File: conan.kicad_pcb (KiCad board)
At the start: 2 copper layers, 307 parts, among them J1 JST-XH, J10 PWM11, J11 PWM3, J12 PWM7, J13 PWM12, J14 PWM4, J15 PWM8, J16 Stepper, J17 Stepper, J18 Stepper, J19 Stepper, J2 JST-XH, J20 Stepper, J21 Stepper, J22 Boot, J23 UART1, J24 UART2, J25 USB_B_Micro, J26 Endstop 1, J27 Endstop 2, J28 Endstop 3, J29 Endstop 4, J3 JTAG, J30 Endstop 5, J31 Endstop 6, J32 Endstop 7, J33 Endstop 8, J34 Watchdog, J35 Thermistor 1, J36 Thermistor 2, J37 Thermistor 3, J38 Thermistor 4, J39 Thermistor 5, J4 PWM9, J40 Thermistor 6, J41 Thermistor 7, J42 Thermistor 8, J43 pmod, J44 esp8266, J45 Chain_in, J46 Chain_out, J47 Exp1_L, J48 Display, J49 Exp1_R, J5 PWM5, J50 Vaux in, J51 VM2 in, J52 VM1 in, J53 Vaux in, J54 Exp2_L, J55 Exp2_R, J6 PWM1_HP, J7 PWM10, J8 PWM2_HP, J9 PWM6, Q1 AON7524, Q2 TPH1R405PL, Q3 TPH1R405PL, Q4 AON7524, Q5 AON7524, Q6 AON7524, Q7 AON7524, Q8 AON7524, Q9 Q_NMOS_DGS, SW1 Reset, U1 ECP5U12_CABGA256, U10 TMC2209, U11 TMC2209, U12 TMC2209, U13 TMC2209, U14 AT25xxx, U15 STM32F070CBTx, U16 74VLX244, U17 STWD100, U2 L7986, U3 TLV62569, U4 TLV62569, U5 LP5907MFX-2.5, U6 LP5907MFX-3.3, U7 MIC4127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

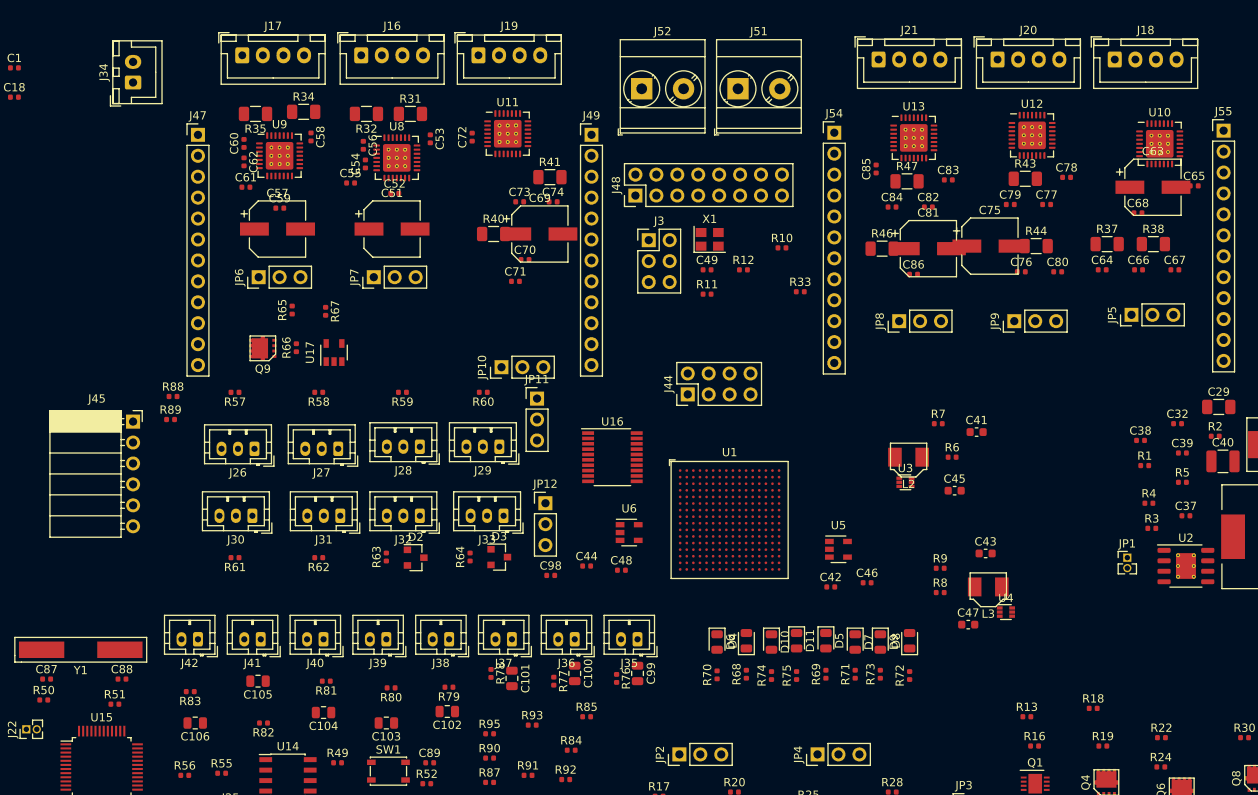
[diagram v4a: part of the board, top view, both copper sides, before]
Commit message: routing sketch for stepper driver
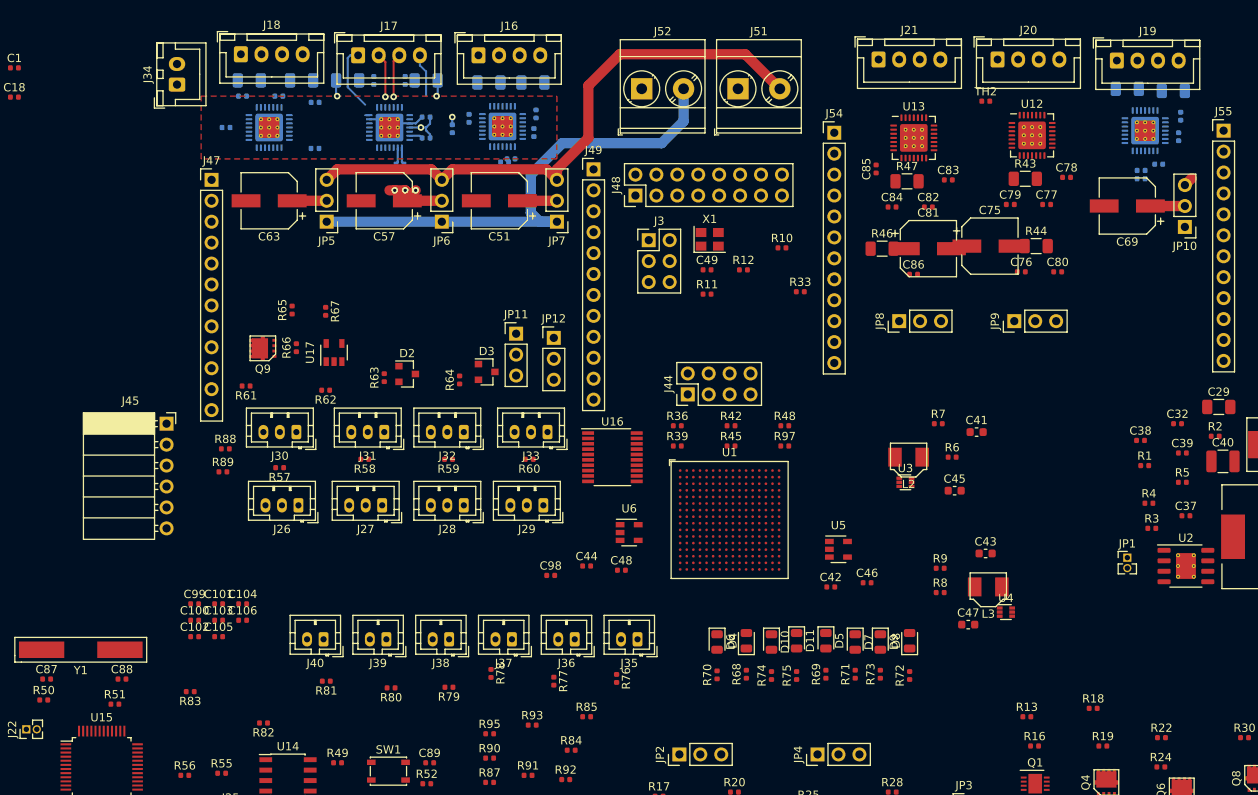
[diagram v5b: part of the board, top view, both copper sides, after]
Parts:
- removed J41: Thermistor 7, Connector_JST:JST_PH_B2B-PH-K_1x02_P2.00mm_Vertical
- removed J42: Thermistor 8, Connector_JST:JST_PH_B2B-PH-K_1x02_P2.00mm_Vertical
- added R36: 1k, Resistor_SMD:R_0402_1005Metric, F.Cu at (115.6, 72.4)
- added R39: 1k, Resistor_SMD:R_0402_1005Metric, F.Cu at (115.6, 74.8)
- added R42: 1k, Resistor_SMD:R_0402_1005Metric, F.Cu at (122.1, 72.4)
- added R45: 1k, Resistor_SMD:R_0402_1005Metric, F.Cu at (122.1, 74.8)
- added R48: 1k, Resistor_SMD:R_0402_1005Metric, F.Cu at (128.6, 72.4)
- added R97: 1k, Resistor_SMD:R_0402_1005Metric, F.Cu at (128.6, 74.8)
- added TH1: NTC_100k, Resistor_SMD:R_0402_1005Metric, B.Cu at (88.3, 36.3)
- added TH2: NTC_100k, Resistor_SMD:R_0402_1005Metric, F.Cu at (153.0, 33.0)
- C100, C101, C102, C103, C104, C99: value 10uF -> 2.2uF; footprint Capacitor_SMD:C_0805_2012Metric -> Capacitor_SMD:C_0402_1005Metric
- C105, C106: value 10uF -> 1uF; footprint Capacitor_SMD:C_0805_2012Metric -> Capacitor_SMD:C_0402_1005Metric
- C52, C53, C54, C55, C56, C58, C59, C60, C61, C62, C64, C65, C66, C67, C68, C70, C71, C72, C73, C74, R31, R32, R34, R35, R37, R38, R40, R41, U10, U11, U8, U9: moved to B.Cu
- moved C65 117.7 mm to (60.8, 36.2), turned to 180 degrees
- moved C67 115.1 mm to (62.8, 32.4), turned to 180 degrees
- moved U10 108.1 mm to (66.0, 36.2), turned to 180 degrees
- moved C63 107.3 mm to (66.0, 45.1), turned to 180 degrees
- moved C66 106.4 mm to (67.2, 32.4), turned to 180 degrees
- moved J18 106.0 mm to (62.6, 27.3)
- moved R37 106.0 mm to (63.6, 30.5), turned to 180 degrees
- moved R38 105.3 mm to (70.0, 30.5), turned to 180 degrees
- moved C68 100.2 mm to (71.6, 38.7), turned to 180 degrees
- moved JP5 98.3 mm to (73.0, 47.6), turned to 180 degrees
- moved C64 97.6 mm to (71.6, 33.1), turned to 180 degrees
- moved C72 86.0 mm to (176.7, 34.8)
- moved JP10 84.7 mm to (177.2, 48.3), turned to 180 degrees
- moved R40 78.9 mm to (170.2, 31.5), turned to 180 degrees
- moved C73 77.7 mm to (174.0, 40.6), turned to 180 degrees
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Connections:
- net Net-(J16-Pad3) renamed /Stepper/Stepper 3/OB1
- net Net-(J16-Pad4) renamed /Stepper/Stepper 3/OB2
- net Net-(J17-Pad3) renamed /Stepper/Stepper 2/OB1
- net Net-(J17-Pad4) renamed /Stepper/Stepper 2/OB2
- net Net-(J18-Pad3) renamed /Stepper/Stepper 1/OB1
- net Net-(J18-Pad4) renamed /Stepper/Stepper 1/OB2
- net Net-(J19-Pad3) renamed /Stepper/Stepper 6/OB1
- net Net-(J19-Pad4) renamed /Stepper/Stepper 6/OB2
- net Net-(J20-Pad3) renamed /Stepper/Stepper 5/OB1
- net Net-(J20-Pad4) renamed /Stepper/Stepper 5/OB2
- net Net-(J21-Pad3) renamed /Stepper/Stepper 4/OB1
- net Net-(J21-Pad4) renamed /Stepper/Stepper 4/OB2
- J16 pad 1: Net-(J16-Pad1) -> /Stepper/Stepper 3/OA1
- J16 pad 2: Net-(J16-Pad2) -> /Stepper/Stepper 3/OA2
- J17 pad 1: Net-(J17-Pad1) -> /Stepper/Stepper 2/OA1
- J17 pad 2: Net-(J17-Pad2) -> /Stepper/Stepper 2/OA2
- J18 pad 1: Net-(J18-Pad1) -> /Stepper/Stepper 1/OA1
- J18 pad 2: Net-(J18-Pad2) -> /Stepper/Stepper 1/OA2
- J19 pad 1: Net-(J19-Pad1) -> /Stepper/Stepper 6/OA1
- J19 pad 2: Net-(J19-Pad2) -> /Stepper/Stepper 6/OA2
- J20 pad 1: Net-(J20-Pad1) -> /Stepper/Stepper 5/OA1
- J20 pad 2: Net-(J20-Pad2) -> /Stepper/Stepper 5/OA2
- J21 pad 1: Net-(J21-Pad1) -> /Stepper/Stepper 4/OA1
- J21 pad 2: Net-(J21-Pad2) -> /Stepper/Stepper 4/OA2
- U10 pad 14: UART1 -> Net-(R42-Pad2)
- U10 pad 21: Net-(J18-Pad1) -> /Stepper/Stepper 1/OA2
- U10 pad 24: Net-(J18-Pad2) -> /Stepper/Stepper 1/OA1
- U11 pad 14: UART6 -> Net-(R45-Pad2)
- U11 pad 21: Net-(J19-Pad1) -> /Stepper/Stepper 6/OA2
- U11 pad 24: Net-(J19-Pad2) -> /Stepper/Stepper 6/OA1
- U12 pad 14: UART5 -> Net-(R48-Pad2)
- U12 pad 21: Net-(J20-Pad1) -> /Stepper/Stepper 5/OA2
- U12 pad 24: Net-(J20-Pad2) -> /Stepper/Stepper 5/OA1
- U13 pad 14: UART4 -> Net-(R97-Pad2)
- U13 pad 21: Net-(J21-Pad1) -> /Stepper/Stepper 4/OA2
- U13 pad 24: Net-(J21-Pad2) -> /Stepper/Stepper 4/OA1
- U8 pad 14: UART3 -> Net-(R36-Pad2)
- U8 pad 21: Net-(J16-Pad1) -> /Stepper/Stepper 3/OA2
- U8 pad 24: Net-(J16-Pad2) -> /Stepper/Stepper 3/OA1
- U9 pad 14: UART2 -> Net-(R39-Pad2)
- U9 pad 21: Net-(J17-Pad1) -> /Stepper/Stepper 2/OA2
- U9 pad 24: Net-(J17-Pad2) -> /Stepper/Stepper 2/OA1
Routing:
- net +VM2: track 0.00 -> 70.8 mm
- net +VM1: track 0.00 -> 61.4 mm
- net /Stepper/Stepper 2/VM: track 0.00 -> 14.1 mm, vias 0 -> 4
- net GND: track 0.00 -> 11.9 mm, vias 0 -> 3
- net /Stepper/Stepper 2/OA1: track 0.00 -> 7.96 mm
- net /Stepper/Stepper 2/OA2: track 0.00 -> 5.88 mm, vias 0 -> 1
- net /Stepper/Stepper 2/OB1: track 0.00 -> 5.33 mm, vias 0 -> 1
- net /Stepper/Stepper 2/OB2: track 0.00 -> 5.27 mm
- net /Stepper/Stepper 6/VM: track 0.00 -> 4.19 mm
- net /Stepper/Stepper 3/VM: track 0.00 -> 4.19 mm
- net /Stepper/Stepper 1/VM: track 0.00 -> 4.19 mm
- net Net-(C61-Pad1): track 0.00 -> 2.10 mm
- net Net-(C60-Pad1): track 0.00 -> 1.62 mm
- added copper zone on In2.Cu, net /Stepper/Stepper 2/VM
- added copper zone on F.Cu, net GND
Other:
- copper layers 2 -> 4
- rule trace_min: 0.2 -> 0.09
- rule via_min_drill: 0.3 -> 0.2
- rule via_min_size: 0.4 -> 0.45

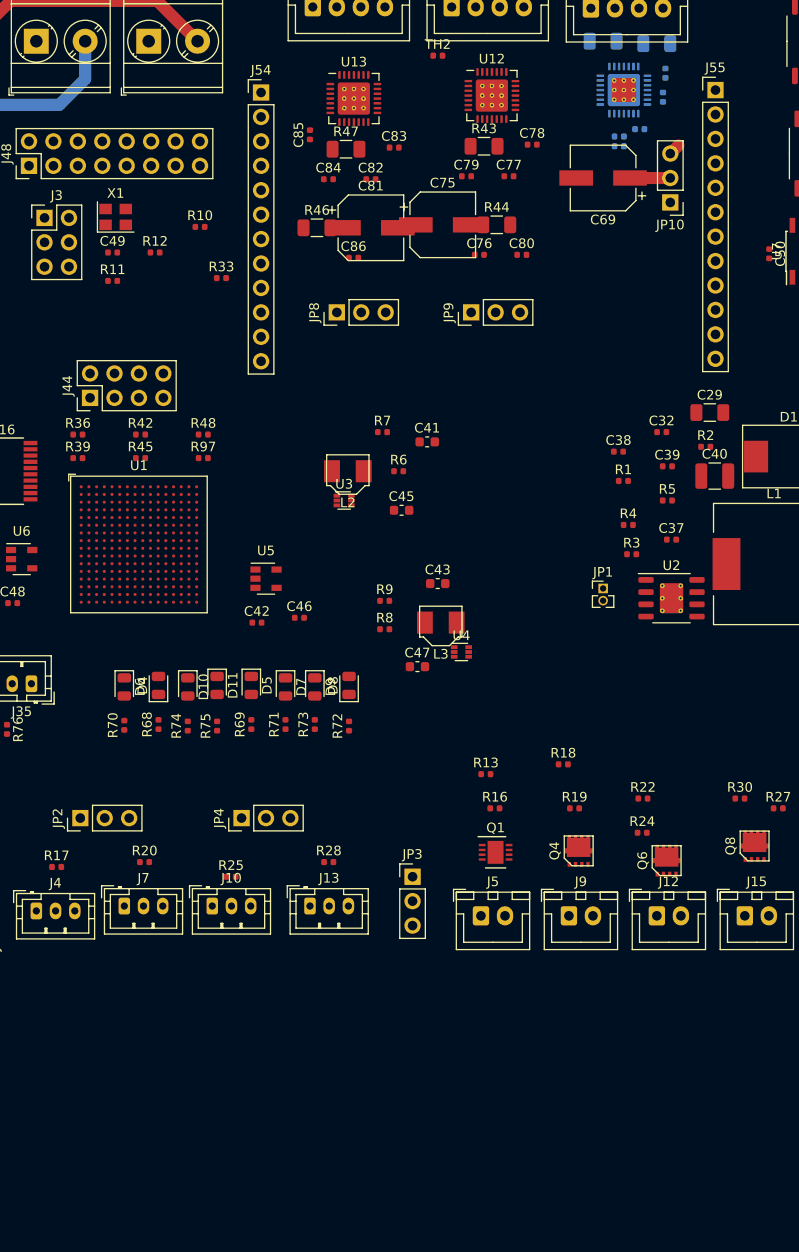
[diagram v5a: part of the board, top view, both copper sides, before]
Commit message: rough reassignment of fpga-pads to account for the direction in which the wires go. Only assign to outer 4 rings for easier escape routing.
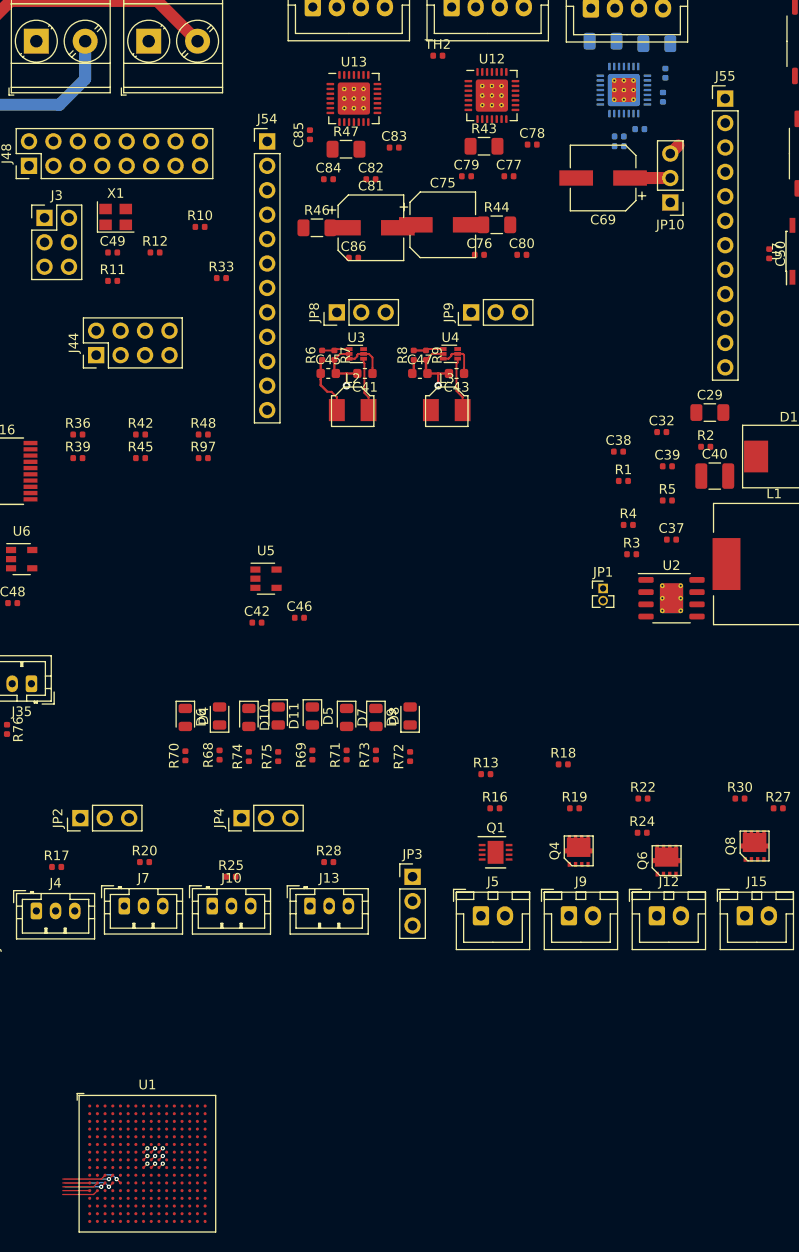
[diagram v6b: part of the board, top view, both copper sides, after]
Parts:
- moved U1 64.4 mm to (122.8, 148.2)
- moved U4 31.0 mm to (154.3, 64.0)
- moved C47 30.5 mm to (151.1, 66.0)
- moved R8 28.7 mm to (150.5, 64.1), turned to 90 degrees
- moved R9 25.9 mm to (151.8, 64.1), turned to 270 degrees
- moved L3 22.1 mm to (153.9, 69.8), turned to 180 degrees
- moved C43 21.9 mm to (154.9, 66.0), turned to 180 degrees
- moved C45 16.1 mm to (141.6, 66.0)
- moved U3 15.3 mm to (144.5, 64.0)
- moved R6 14.5 mm to (141.0, 64.1), turned to 90 degrees
- moved C41 9.62 mm to (145.4, 66.0), turned to 180 degrees
- moved R7 9.44 mm to (142.2, 64.1), turned to 270 degrees
- moved R68 7.10 mm to (130.3, 105.7)
- moved R69 7.10 mm to (140.0, 105.7)
- moved R71 7.10 mm to (143.5, 105.7)
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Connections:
- U1 pad A10: UART6 -> Net-(U1-PadA10)
- U1 pad A11: PWM11 -> Net-(U1-PadA11)
- U1 pad A12: PWM9 -> Net-(U1-PadA12)
- U1 pad A4: Net-(U1-PadA4) -> DIAG3
- U1 pad A5: Net-(U1-PadA5) -> display10
- U1 pad A6: Net-(U1-PadA6) -> display9
- U1 pad A7: Net-(U1-PadA7) -> display3
- U1 pad A8: Net-(U1-PadA8) -> display1
- U1 pad A9: FPGA2 -> Net-(U1-PadA9)
- U1 pad B1: ENDSTOP1 -> DIR1
- U1 pad B10: FPGA1 -> Net-(U1-PadB10)
- U1 pad B11: UART3 -> Net-(U1-PadB11)
- U1 pad B12: PWM8 -> Net-(U1-PadB12)
- U1 pad B13: PWM4 -> ESP_EN
- U1 pad B15: display13 -> exp2_16
- U1 pad B16: Net-(U1-PadB16) -> exp2_17
- U1 pad B2: ENDSTOP2 -> STEP1
- U1 pad B3: Net-(U1-PadB3) -> INDEX3
- U1 pad B4: Net-(U1-PadB4) -> DIAG1
- U1 pad B5: Net-(U1-PadB5) -> display11
- U1 pad B6: Net-(U1-PadB6) -> display6
- U1 pad B7: Net-(U1-PadB7) -> display2
- U1 pad B8: WDI -> Net-(U1-PadB8)
- U1 pad B9: FPGA6 -> Net-(U1-PadB9)
- U1 pad C1: ENDSTOP5 -> DIR3
- U1 pad C10: UART5 -> Net-(U1-PadC10)
- U1 pad C11: UART1 -> Net-(U1-PadC11)
- U1 pad C12: PWM6 -> ESP_GPIO2
- U1 pad C13: PWM2 -> ESP_RX
- U1 pad C14: display12 -> exp2_15
- U1 pad C15: display8 -> exp2_11
- U1 pad C16: display10 -> exp2_13
- U1 pad C2: ENDSTOP7 -> UART1
- U1 pad C3: ENDSTOP3 -> DIR2
- U1 pad C4: Net-(U1-PadC4) -> DIAG2
- U1 pad C5: Net-(U1-PadC5) -> display13
- U1 pad C6: Net-(U1-PadC6) -> display7
- U1 pad C7: Net-(U1-PadC7) -> display4
- U1 pad C8: CLK -> Net-(U1-PadC8)
- U1 pad C9: FPGA4 -> Net-(U1-PadC9)
- U1 pad D1: LED1 -> UART3
- U1 pad D10: UART4 -> Net-(U1-PadD10)
- U1 pad D11: PWM12 -> Net-(U1-PadD11)
- U1 pad D12: PWM7 -> Net-(U1-PadD12)
- U1 pad D13: PWM3 -> ESP_RST
- U1 pad D14: display11 -> exp2_14
- U1 pad D16: display6 -> exp2_9
- U1 pad D3: ENDSTOP4 -> STEP2
- U1 pad D4: Net-(U1-PadD4) -> INDEX1
- U1 pad D5: Net-(U1-PadD5) -> display12
- U1 pad D6: Net-(U1-PadD6) -> display8
- U1 pad D7: Net-(U1-PadD7) -> display5
- U1 pad D8: WDEN -> Net-(U1-PadD8)
- U1 pad D9: FPGA5 -> Net-(U1-PadD9)
- U1 pad E1: LED8 -> exp1_7
- U1 pad E10: UART2 -> Net-(U1-PadE10)
- U1 pad E11: PWM10 -> Net-(U1-PadE11)
- U1 pad E12: PWM5 -> ESP_FLASH
- U1 pad E13: PWM1 -> ESP_TX
- U1 pad E14: display9 -> exp2_12
- U1 pad E15: display4 -> exp2_7
- U1 pad E16: pmod2_2 -> exp2_2
- U1 pad E2: LED3 -> exp1_2
- U1 pad E3: ENDSTOP6 -> STEP3
- U1 pad E4: Net-(U1-PadE4) -> INDEX2
- U1 pad E8: ENN -> Net-(U1-PadE8)
- U1 pad E9: FPGA3 -> Net-(U1-PadE9)
- U1 pad F1: DIR1 -> exp1_8
- U1 pad F12: display3 -> exp2_6
- U1 pad F13: display5 -> exp2_8
- U1 pad F14: display7 -> exp2_10
- U1 pad F15: display1 -> exp2_4
- U1 pad F16: pmod2_3 -> exp2_1
- U1 pad F2: LED6 -> exp1_5
- U1 pad F3: ENDSTOP8 -> UART2
- U1 pad F4: LED2 -> exp1_1
- U1 pad F5: LED4 -> exp1_3
- U1 pad G1: STEP5 -> exp1_14
- U1 pad G12: display2 -> exp2_5
- U1 pad G13: pmod2_1 -> exp2_3
- U1 pad G14: pmod2_4 -> DIAG6
- U1 pad G15: pmod1_4 -> INDEX6
- U1 pad G16: chain_in_in3 -> UART5
- U1 pad G2: DIR2 -> exp1_10
- U1 pad G3: STEP1 -> exp1_9
- U1 pad G4: LED7 -> exp1_6
- U1 pad G5: LED5 -> exp1_4
- U1 pad H12: pmod1_2 -> INDEX5
- U1 pad H13: chain_in_in1 -> INDEX4
- U1 pad H14: pmod1_3 -> DIAG5
- U1 pad H15: chain_in_out2 -> DIR6
- U1 pad H2: STEP6 -> exp1_16
- U1 pad H3: STEP2 -> exp1_11
- U1 pad H4: STEP4 -> exp1_13
- U1 pad H5: DIR3 -> Net-(U1-PadH5)
- U1 pad J1: Net-(U1-PadJ1) -> WDI
- U1 pad J12: chain_in_in2 -> UART6
- U1 pad J13: pmod1_1 -> DIAG4
- U1 pad J14: chain_in_out1 -> UART4
- U1 pad J15: chain_out_out2 -> DIR4
- U1 pad J16: chain_out_in1 -> DIR5
- U1 pad J2: Net-(U1-PadJ2) -> CLK
- U1 pad J3: DIR5 -> exp1_15
- U1 pad J4: STEP3 -> exp1_12
- U1 pad J5: DIR4 -> Net-(U1-PadJ5)
- U1 pad K1: Net-(U1-PadK1) -> WDEN
- U1 pad K12: Net-(U1-PadK12) -> pmod1_2
- U1 pad K13: Net-(U1-PadK13) -> pmod1_4
- U1 pad K14: chain_out_in2 -> STEP6
- U1 pad K15: chain_out_out1 -> STEP4
- U1 pad K16: chain_out_out3 -> STEP5
- U1 pad K2: Net-(U1-PadK2) -> ENN
- U1 pad K3: DIR6 -> exp1_17
- U1 pad K4: exp2_5 -> PWM5
- U1 pad K5: exp2_7 -> PWM7
- U1 pad L1: exp2_1 -> PWM1
- U1 pad L12: Net-(U1-PadL12) -> pmod1_1
- U1 pad L13: Net-(U1-PadL13) -> pmod1_3
- U1 pad L14: ESP_GPIO2 -> chain_in_in2
- U1 pad L15: Net-(U1-PadL15) -> pmod2_3
- U1 pad L16: Net-(U1-PadL16) -> pmod2_1
- U1 pad L2: exp2_3 -> PWM3
- U1 pad L3: exp2_10 -> PWM10
- U1 pad L4: exp2_6 -> PWM6
- U1 pad L5: exp2_8 -> PWM8
- U1 pad M1: exp2_2 -> PWM2
- U1 pad M11: exp1_4 -> Net-(U1-PadM11)
- U1 pad M12: exp1_7 -> ENDSTOP1
- U1 pad M13: ESP_RX -> chain_out_in2
- U1 pad M14: ESP_EN -> chain_in_out1
- U1 pad M15: Net-(U1-PadM15) -> pmod2_4
- U1 pad M16: Net-(U1-PadM16) -> pmod2_2
- U1 pad M2: exp2_4 -> PWM4
- U1 pad M3: exp2_12 -> PWM12
- U1 pad M4: exp2_14 -> FPGA2
- U1 pad M5: INDEX5 -> Net-(U1-PadM5)
- U1 pad M6: DIAG6 -> Net-(U1-PadM6)
- U1 pad N1: exp2_9 -> PWM9
- U1 pad N11: exp1_3 -> Net-(U1-PadN11)
- U1 pad N12: exp1_5 -> Net-(U1-PadN12)
- U1 pad N13: exp1_16 -> chain_out_out2
- U1 pad N14: exp1_17 -> chain_out_out3
- U1 pad N16: Net-(U1-PadN16) -> chain_in_in1
- U1 pad N3: exp2_16 -> FPGA4
- U1 pad N4: exp2_17 -> FPGA5
- U1 pad N5: INDEX6 -> Net-(U1-PadN5)
- U1 pad P1: exp2_13 -> FPGA1
- U1 pad P11: exp1_2 -> Net-(U1-PadP11)
- U1 pad P12: exp1_1 -> Net-(U1-PadP12)
- U1 pad P13: exp1_12 -> ENDSTOP6
- U1 pad P14: exp1_14 -> ENDSTOP8
- U1 pad P15: ESP_FLASH -> chain_in_in3
- U1 pad P16: ESP_RST -> chain_in_out2
- U1 pad P2: exp2_11 -> PWM11
- U1 pad P3: INDEX1 -> LED1
- U1 pad P4: INDEX2 -> LED3
- U1 pad R1: exp2_15 -> FPGA3
- U1 pad R12: exp1_8 -> ENDSTOP2
- U1 pad R13: exp1_11 -> ENDSTOP5
- U1 pad R14: exp1_10 -> ENDSTOP4
- U1 pad R15: exp1_15 -> chain_out_out1
- U1 pad R16: ESP_TX -> chain_out_in1
- U1 pad R2: DIAG1 -> FPGA6
- U1 pad R3: INDEX3 -> LED5
- U1 pad R4: DIAG3 -> LED4
- U1 pad R5: DIAG4 -> LED7
- U1 pad T13: exp1_6 -> Net-(U1-PadT13)
- U1 pad T14: exp1_9 -> ENDSTOP3
- U1 pad T15: exp1_13 -> ENDSTOP7
- U1 pad T2: DIAG2 -> LED2
- U1 pad T3: INDEX4 -> LED6
- U1 pad T4: DIAG5 -> LED8
- U4 pad 5: Net-(U4-Pad5) -> +5V
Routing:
- net GND: track 11.9 -> 30.2 mm, vias 3 -> 13
- net +5V: track 0.00 -> 8.96 mm
- net +1V1: track 0.00 -> 6.80 mm, vias 0 -> 1
- net Net-(L3-Pad1): track 0.00 -> 5.66 mm
- net Net-(L2-Pad1): track 0.00 -> 5.56 mm
- net PWM6: track 0.00 -> 5.36 mm, vias 0 -> 1
- net PWM5: track 0.00 -> 5.17 mm, vias 0 -> 1
- net exp1_17: track 0.00 -> 4.57 mm
- net PWM10: track 0.00 -> 4.37 mm, vias 0 -> 1
- net PWM4: track 0.00 -> 3.77 mm
- net PWM3: track 0.00 -> 3.77 mm
- net Net-(R8-Pad2): track 0.00 -> 3.12 mm
- net Net-(R6-Pad2): track 0.00 -> 2.86 mm
- net PWM2: track 0.00 -> 2.80 mm
- net PWM1: track 0.00 -> 2.80 mm
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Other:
- net class Default: clearance 0.2 -> 0.15
- rule trace_clearance: 0.2 -> 0.15

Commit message: more reassignments
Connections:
- U1 pad A10: Net-(U1-PadA10) -> chain_in_in3
- U1 pad A9: Net-(U1-PadA9) -> chain_in_in1
- U1 pad B10: Net-(U1-PadB10) -> chain_in_in2
- U1 pad B15: exp2_16 -> exp2_12
- U1 pad B16: exp2_17 -> exp2_13
- U1 pad C10: Net-(U1-PadC10) -> chain_in_out1
- U1 pad C14: exp2_15 -> exp2_11
- U1 pad C15: exp2_11 -> exp2_7
- U1 pad C16: exp2_13 -> exp2_9
- U1 pad D10: Net-(U1-PadD10) -> chain_in_out2
- U1 pad D14: exp2_14 -> exp2_10
- U1 pad D16: exp2_9 -> exp2_5
- U1 pad E14: exp2_12 -> exp2_8
- U1 pad E15: exp2_7 -> exp2_3
- U1 pad E16: exp2_2 -> DIAG6
- U1 pad F12: exp2_6 -> Net-(U1-PadF12)
- U1 pad F13: exp2_8 -> exp2_4
- U1 pad F14: exp2_10 -> exp2_6
- U1 pad F15: exp2_4 -> exp2_2
- U1 pad F16: exp2_1 -> INDEX6
- U1 pad G12: exp2_5 -> Net-(U1-PadG12)
- U1 pad G13: exp2_3 -> exp2_1
- U1 pad G14: DIAG6 -> DIAG5
- U1 pad G15: INDEX6 -> INDEX5
- U1 pad H12: INDEX5 -> Net-(U1-PadH12)
- U1 pad H13: INDEX4 -> UART6
- U1 pad H14: DIAG5 -> DIAG4
- U1 pad J12: UART6 -> Net-(U1-PadJ12)
- U1 pad J13: DIAG4 -> INDEX4
- U1 pad K12: pmod1_2 -> Net-(U1-PadK12)
- U1 pad K5: PWM7 -> Net-(U1-PadK5)
- U1 pad L12: pmod1_1 -> Net-(U1-PadL12)
- U1 pad L14: chain_in_in2 -> pmod1_1
- U1 pad L3: PWM10 -> PWM8
- U1 pad L5: PWM8 -> Net-(U1-PadL5)
- U1 pad M12: ENDSTOP1 -> Net-(U1-PadM12)
- U1 pad M13: chain_out_in2 -> chain_out_out2
- U1 pad M14: chain_in_out1 -> chain_out_in1
- U1 pad M3: PWM12 -> PWM10
- U1 pad N1: PWM9 -> PWM7
- U1 pad N12: Net-(U1-PadN12) -> exp2_14
- U1 pad N13: chain_out_out2 -> ENDSTOP7
- U1 pad N14: chain_out_out3 -> ENDSTOP8
- U1 pad N16: chain_in_in1 -> pmod1_2
- U1 pad P11: Net-(U1-PadP11) -> PWM12
- U1 pad P12: Net-(U1-PadP12) -> PWM11
- U1 pad P13: ENDSTOP6 -> ENDSTOP3
- U1 pad P14: ENDSTOP8 -> ENDSTOP5
- U1 pad P15: chain_in_in3 -> chain_out_in2
- U1 pad P16: chain_in_out2 -> chain_out_out3
- U1 pad P2: PWM11 -> PWM9
- U1 pad R12: ENDSTOP2 -> exp2_16
- U1 pad R13: ENDSTOP5 -> ENDSTOP2
- U1 pad R14: ENDSTOP4 -> ENDSTOP1
- U1 pad R15: chain_out_out1 -> ENDSTOP6
- U1 pad R16: chain_out_in1 -> chain_out_out1
- U1 pad T13: Net-(U1-PadT13) -> exp2_15
- U1 pad T14: ENDSTOP3 -> exp2_17
- U1 pad T15: ENDSTOP7 -> ENDSTOP4
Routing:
- net PWM10: track 4.37 -> 0.00 mm, vias 1 -> 0
- net PWM8: track 1.91 -> 4.37 mm

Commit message: clean start for escape routing
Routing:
- net PWM6: track 5.36 -> 0.00 mm, vias 1 -> 0
- net PWM5: track 5.17 -> 0.00 mm, vias 1 -> 0
- net exp1_17: track 4.57 -> 0.00 mm
- net GND: track 30.2 -> 25.7 mm, vias 13 -> 5
- net PWM8: track 4.37 -> 0.00 mm, vias 1 -> 0
- net PWM4: track 3.77 -> 0.00 mm
- net PWM3: track 3.77 -> 0.00 mm
- net PWM2: track 2.80 -> 0.00 mm
- net PWM1: track 2.80 -> 0.00 mm
- net +1V1: track 6.80 -> 6.24 mm, vias 1 -> 0
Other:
- net class Default: clearance 0.15 -> 0.1
- rule trace_clearance: 0.15 -> 0.1
